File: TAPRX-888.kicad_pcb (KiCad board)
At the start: 6 copper layers, 83.5 x 99.4 mm, 225 parts, among them J1 CONN_SMA_JACK_EDGE_JLC_With_N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, J10 U.FL-R, J11 Conn_JTAG10-mini, J2 CONN_SMA_JACK_EDGE_JLC_With_N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, J3 CONN_SMA_JACK_EDGE_JLC_With_N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, J4 CONN_SMA_JACK_EDGE_JLC_With_N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, J5 USB-3.0, J6 Conn_01x03, J7 Conn_01x03, J8 Conn_01x03, J9 Conn_01x03, Q1 PMOS Si2343DS, Q2 MMBT3904, Q3 PMOS Si2343DS, U1 AP2114H-3.3TRG1, U10 XO-19.2MHZ, U11 CYUSB3014-BZXCT, U12 BAV99, U13 BAV99, U14 LP5907MFX-3.3, U15 BAV99, U16 TLV3501, U17 BAV99, U18 NC7SV157, U19 74LVC2G14, U2 AP2114H-3.3TRG1, U20 Si5351A, U21 NC7SV157, U22 SN65LVDS1, U3 AP2114H-3.3TRG1, U4 LP5907MFX-3.3, U5 UMW AMS1117-1.2, U6 AD8370, U7 TVS-SP3011, U8 LTC2208CUP#PBF, U9 MX25L3233FM2I, X1 TCXO-27M

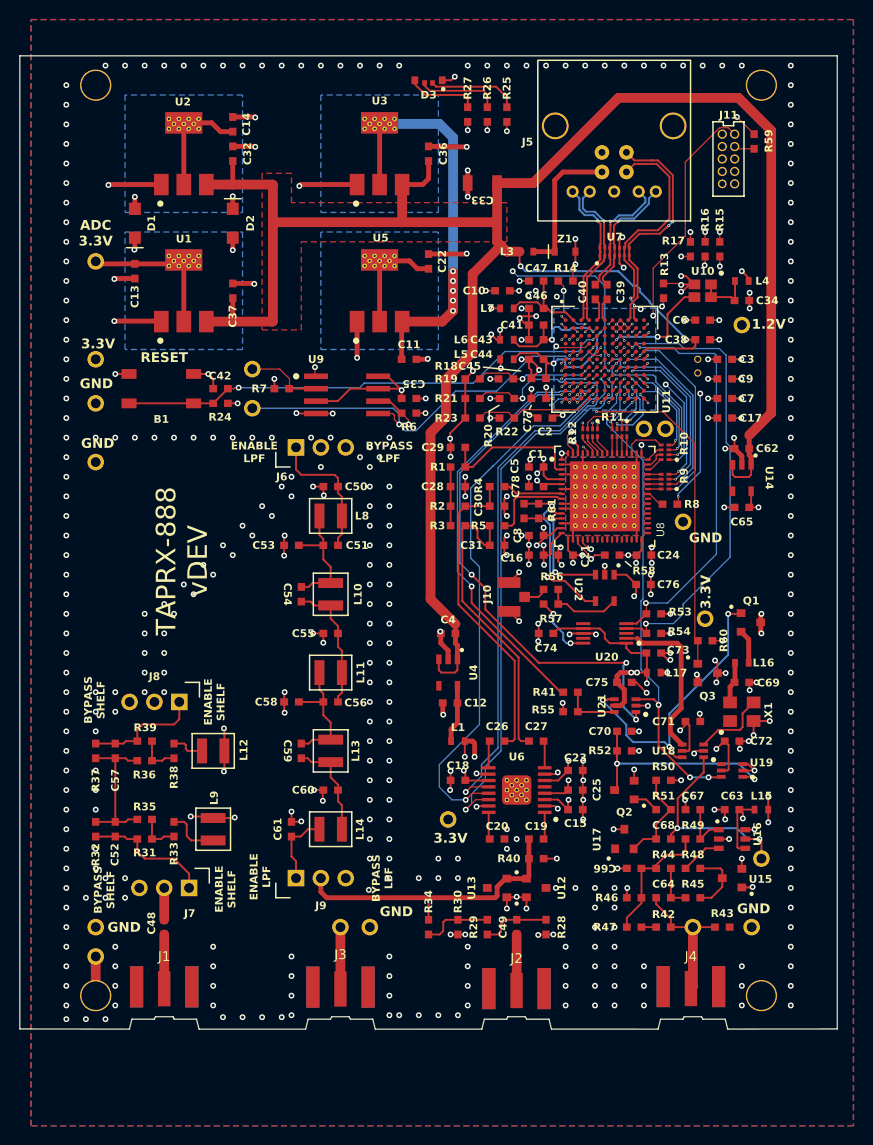
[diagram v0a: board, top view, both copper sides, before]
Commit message: making JLCDFM happy pt. 1
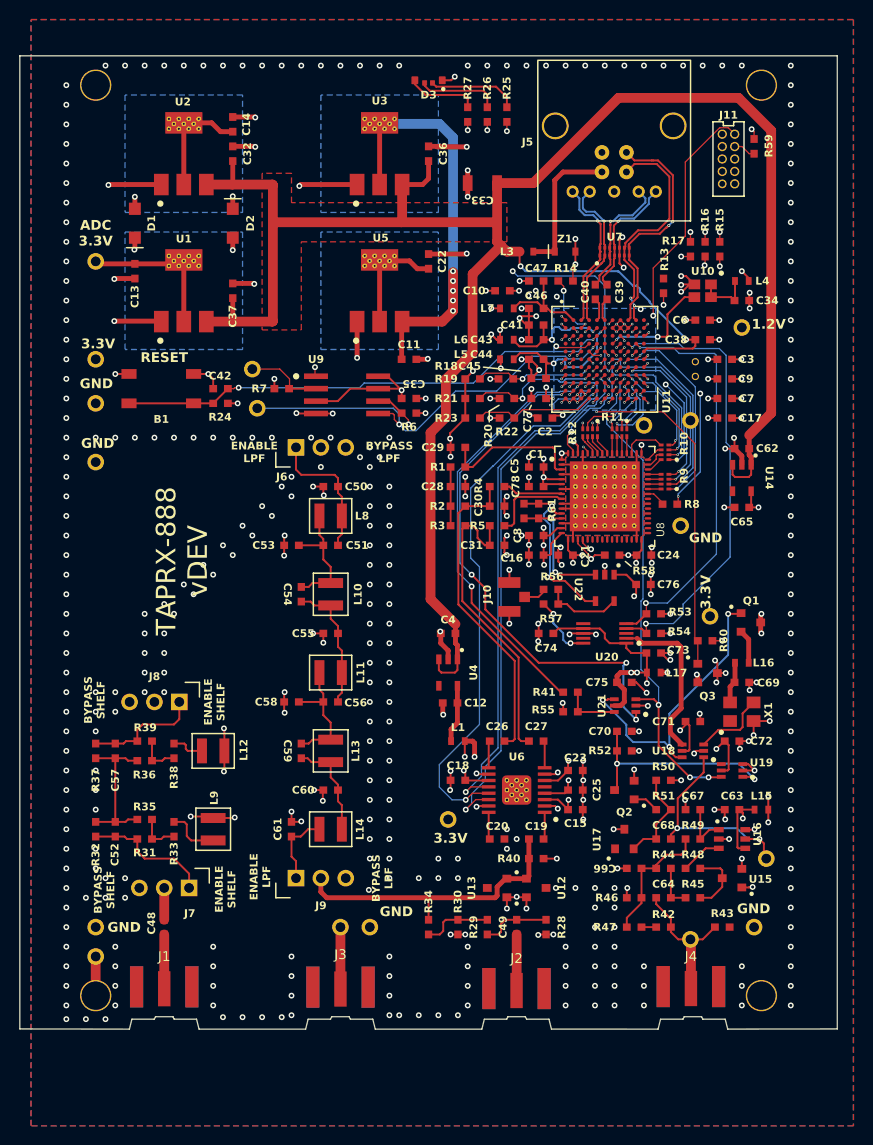
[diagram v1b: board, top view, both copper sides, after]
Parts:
- moved TP12 2.69 mm to (164.8, 87.2)
- moved TP15 1.27 mm to (164.8, 140.2)
- moved TP17 0.56 mm to (166.8, 107.2)
- moved R13 0.50 mm to (162.0, 73.5)
- moved R59 0.50 mm to (171.2, 59.2)
- moved TP10 0.50 mm to (120.5, 86.0)
- moved TP18 0.50 mm to (172.5, 132.0)
- moved TP19 0.47 mm to (163.8, 98.0)
- moved TP21 0.43 mm to (165.2, 82.8)
- moved TP20 0.35 mm to (165.2, 81.2)
- moved TP11 0.35 mm to (160.0, 87.8)
- moved TP16 0.25 mm to (171.2, 139.0)
- moved TP6 0.25 mm to (170.0, 77.8)
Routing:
- net Net-(U11-GPIO19): track 8.19 -> 10.4 mm
- net GND: track 242.8 -> 241.0 mm
- net +3V3: track 49.6 -> 48.2 mm
- net +3V3ADC: track 45.3 -> 44.4 mm, vias 16 -> 14
- net /TRST: track 28.4 -> 28.9 mm
- net Net-(U11-R_USB2): track 8.02 -> 8.52 mm
- net /SPI_MOSI: track 43.6 -> 43.1 mm

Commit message: Q1/Q3 D/S swap, TP11, TP12 to TPTiny and relocate
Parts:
- TP11, TP12: footprint Library:TP -> Library:TP-Tiny
- moved TP12 2.69 mm to (162.2, 88.1)
- moved TP11 0.35 mm to (160.0, 88.1)
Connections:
- L16 pad 2: Net-(Q1-S) -> Net-(Q1-D)
- Q1 pad 2: Net-(Q1-S) -> 3V3REF
- Q1 pad 3: 3V3REF -> Net-(Q1-D)
- Q3 pad 2: /Clock/Vdd5351 -> 3V3REF
- Q3 pad 3: 3V3REF -> /Clock/Vdd5351
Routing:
- net Net-(Q1-D): track 0.00 -> 4.63 mm
- net Net-(Q1-S): track 3.50 -> 0.00 mm
- net 3V3REF: track 12.3 -> 8.92 mm, vias 10 -> 7
- net /Clock/Vdd5351: track 4.62 -> 7.73 mm
- net Net-(U11-GPIO19): track 10.4 -> 8.19 mm
